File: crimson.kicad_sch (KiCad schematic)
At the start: 184 parts, among them J1 Conn_01x02_Socket, SW1 SW_Push_Shielded, SW10 SW_Push_Shielded, SW11 SW_Push_Shielded, SW12 SW_Push_Shielded, SW13 SW_Push_Shielded, SW14 SW_Push_Shielded, SW15 SW_Push_Shielded, SW16 SW_Push_Shielded, SW17 SW_Push_Shielded, SW18 SW_Push_Shielded, SW19 SW_Push_Shielded, SW2 SW_Push_Shielded, SW20 SW_Push_Shielded, SW21 SW_Push_Shielded, SW22 SW_Push_Shielded, SW23 SW_Push_Shielded, SW24 SW_Push_Shielded, SW25 SW_Push_Shielded, SW26 SW_Push_Shielded, SW27 SW_Push_Shielded, SW28 SW_Push_Shielded, SW29 SW_Push_Shielded, SW3 SW_Push_Shielded, SW30 SW_Push_Shielded, SW31 SW_Push_Shielded, SW32 SW_Push_Shielded, SW33 SW_Push_Shielded, SW34 SW_Push_Shielded, SW35 SW_Push_Shielded, SW36 SW_Push_Shielded, SW37 SW_Push_Shielded, SW38 SW_Push_Shielded, SW39 SW_Push_Shielded, SW4 SW_Push_Shielded, SW40 SW_Push_Shielded, SW41 SW_Push_Shielded, SW42 SW_Push_Shielded, SW43 SW_Push_Shielded, SW44 SW_Push_Shielded, SW45 SW_Push_Shielded, SW46 SW_Push_Shielded, SW47 SW_Push_Shielded, SW48 SW_Push_Shielded, SW49 SW_Push_Shielded, SW5 SW_Push_Shielded, SW50 SW_Push_Shielded, SW51 SW_Push_Shielded, SW52 SW_Push_Shielded, SW53 SW_Push_Shielded, SW54 SW_Push_Shielded, SW55 SW_Push_Shielded, SW56 SW_Push_Shielded, SW57 SW_Push_Shielded, SW58 SW_Push_Shielded, SW59 SW_Push_Shielded, SW6 SW_Push_Shielded, SW60 SW_Push_Shielded, SW61 SW_Push_Shielded, SW62 SW_Push_Shielded, SW63 SW_Push_Shielded, SW64 SW_Push_Shielded, SW65 SW_Push_Shielded, SW66 SW_Push_Shielded, SW67 SW_Push_Shielded, SW68 SW_Push_Shielded, SW69 SW_Push_Shielded, SW7 SW_Push_Shielded, SW70 SW_Push_Shielded, SW71 SW_Push_Shielded, SW72 SW_Push_Shielded, SW73 SW_Push_Shielded, SW74 SW_Push_Shielded, SW75 SW_Push_Shielded, SW76 SW_Push_Shielded, SW77 SW_Push_Shielded, SW78 SW_Push_Shielded, SW79 SW_Push_Shielded, SW8 SW_Push_Shielded, SW80 SW_Push_Shielded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

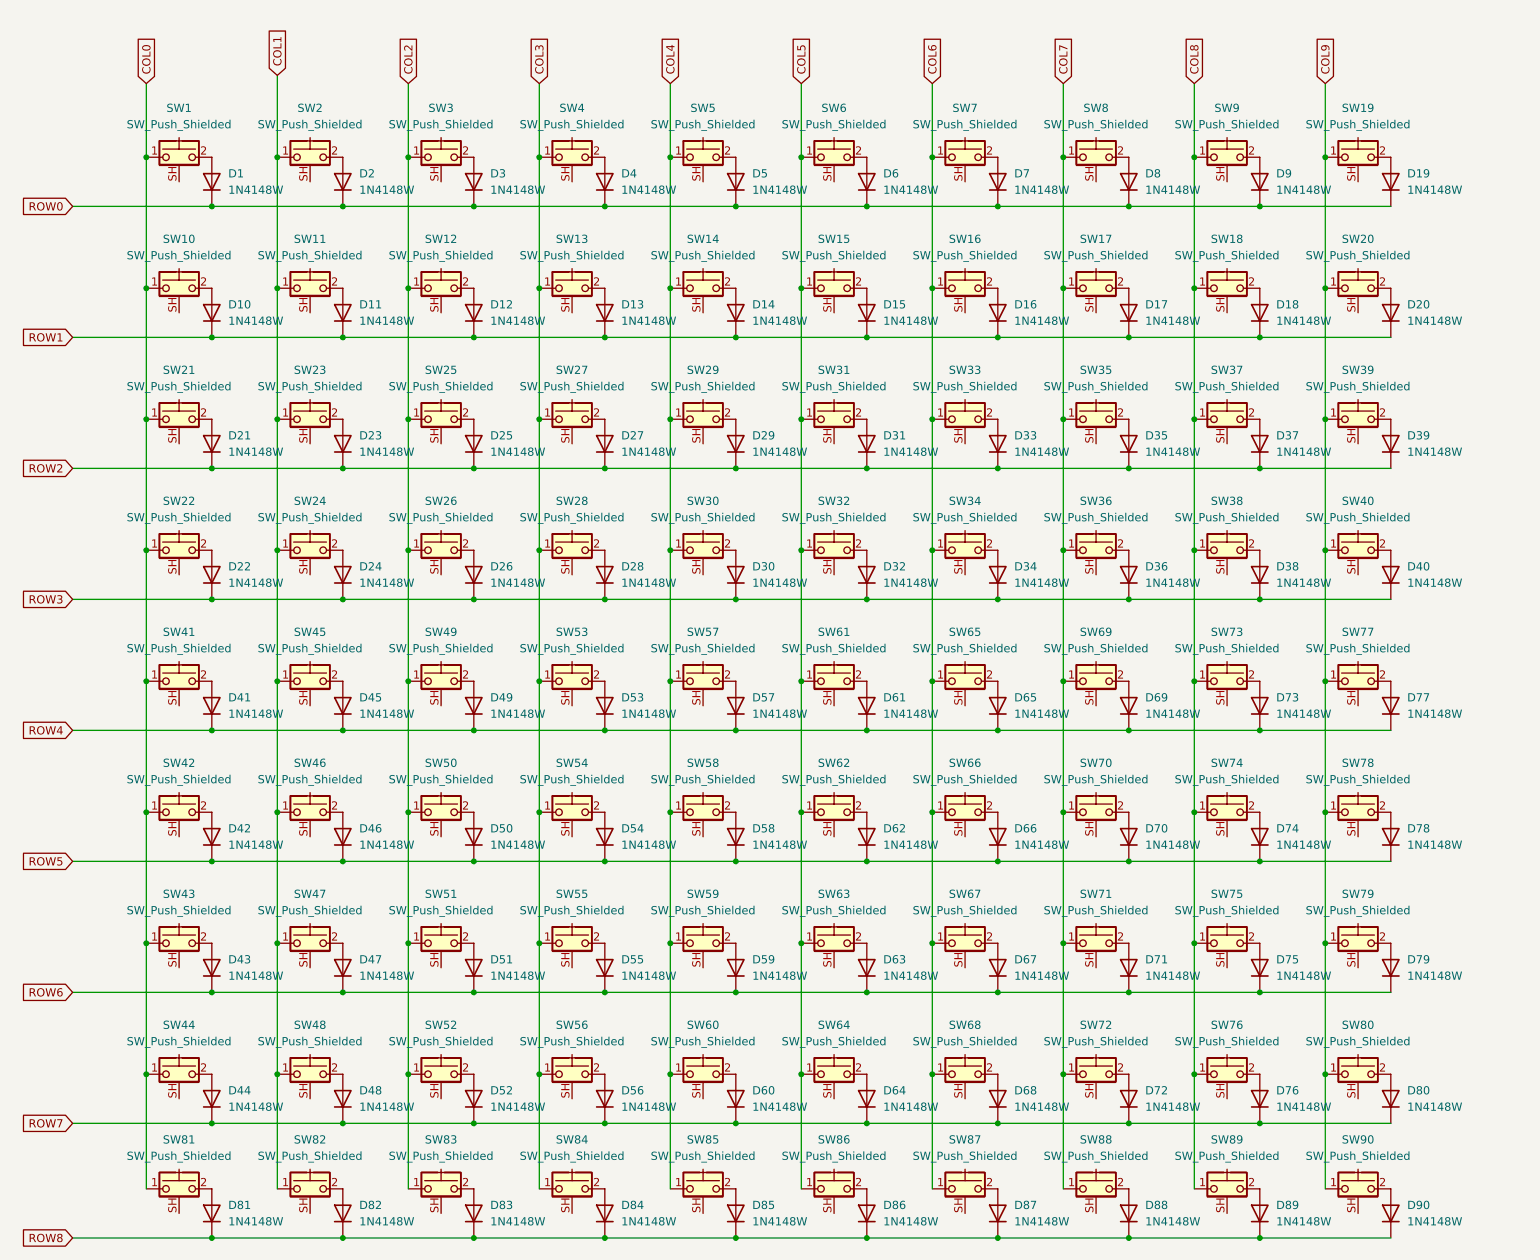
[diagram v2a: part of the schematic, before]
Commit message: [schematics] Add labels for default layout
Default layout will be ANSI QWERTY, so I labeled
the keys accordingly, just so I have a better overview
of things. Layout can be changed later on to stuff like
DVORAK or sth

Signed-off-by: Lucy Mielke <user@domain.tld>
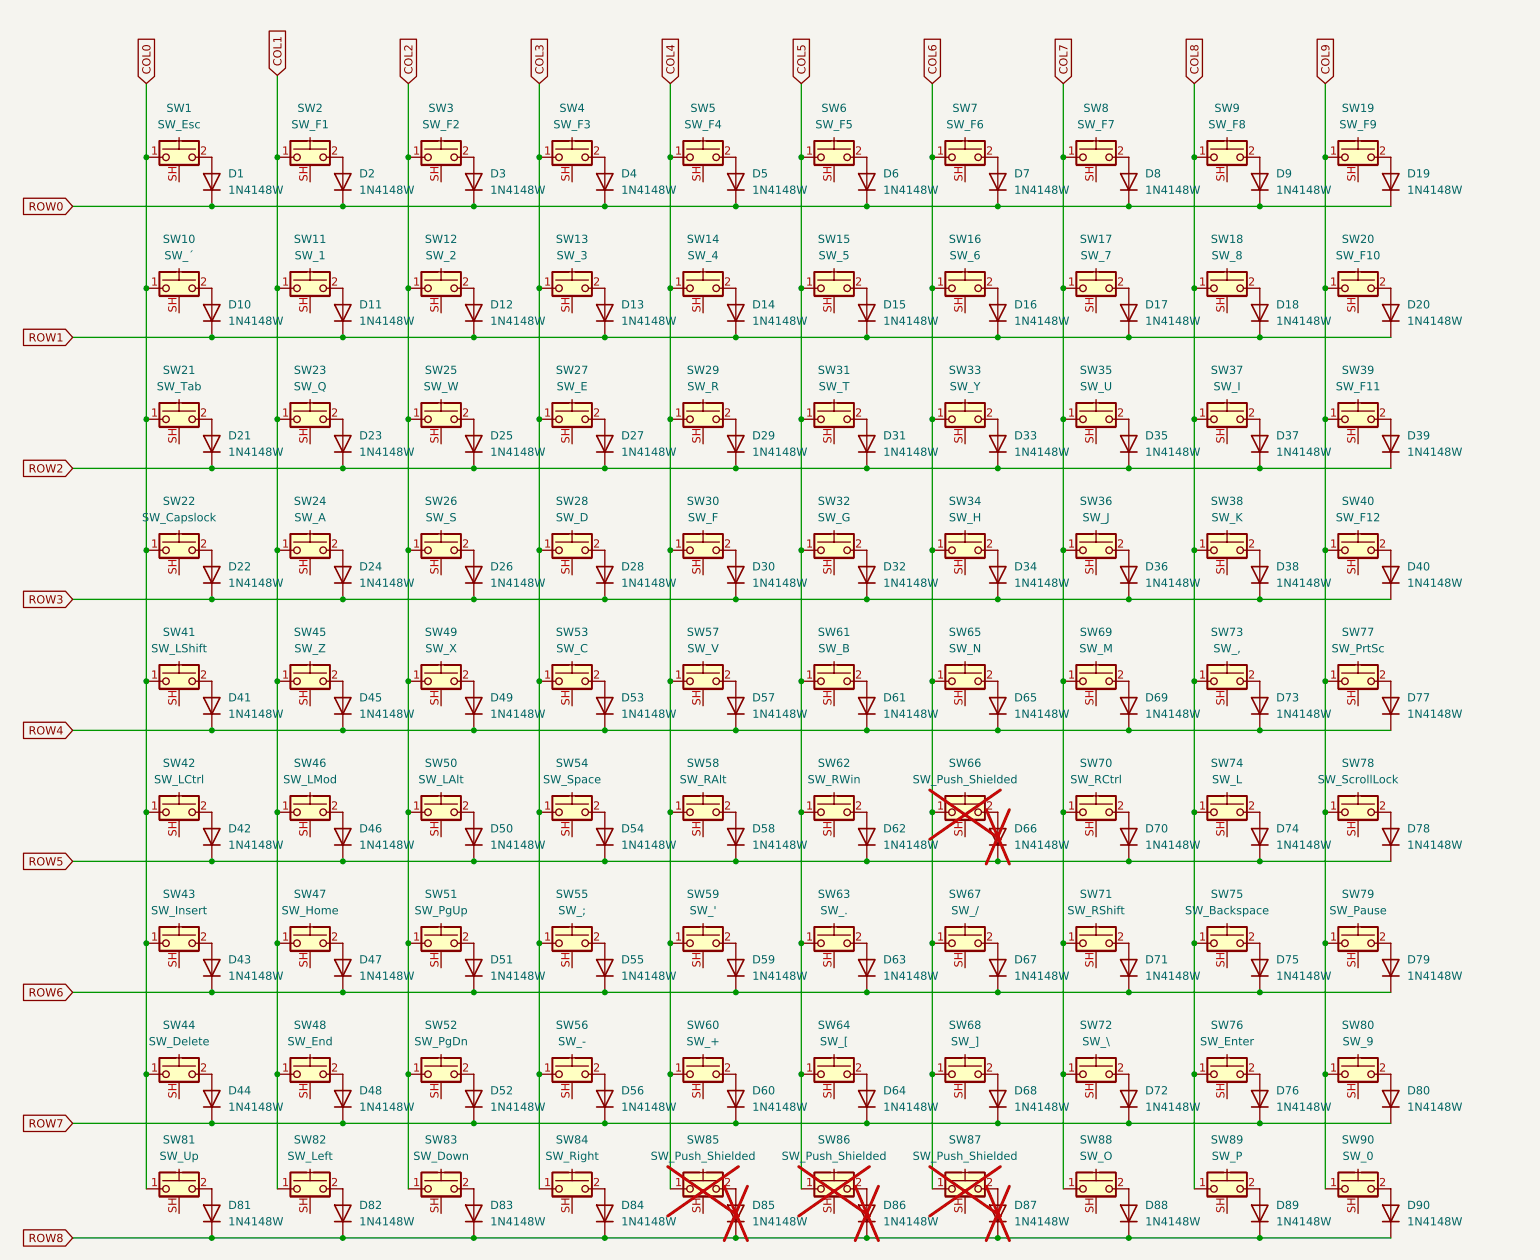
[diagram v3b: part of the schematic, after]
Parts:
- D66, D85, D86, D87, SW66, SW85, SW86, SW87: now not fitted
- SW1: value SW_Push_Shielded -> SW_Esc
- SW10: value SW_Push_Shielded -> SW_´
- SW11: value SW_Push_Shielded -> SW_1
- SW12: value SW_Push_Shielded -> SW_2
- SW13: value SW_Push_Shielded -> SW_3
- SW14: value SW_Push_Shielded -> SW_4
- SW15: value SW_Push_Shielded -> SW_5
- SW16: value SW_Push_Shielded -> SW_6
- SW17: value SW_Push_Shielded -> SW_7
- SW18: value SW_Push_Shielded -> SW_8
- SW19: value SW_Push_Shielded -> SW_F9
- SW2: value SW_Push_Shielded -> SW_F1
- SW20: value SW_Push_Shielded -> SW_F10
- SW21: value SW_Push_Shielded -> SW_Tab
- SW22: value SW_Push_Shielded -> SW_Capslock
- SW23: value SW_Push_Shielded -> SW_Q
- SW24: value SW_Push_Shielded -> SW_A
- SW25: value SW_Push_Shielded -> SW_W
- SW26: value SW_Push_Shielded -> SW_S
- SW27: value SW_Push_Shielded -> SW_E
- SW28: value SW_Push_Shielded -> SW_D
- SW29: value SW_Push_Shielded -> SW_R
- SW3: value SW_Push_Shielded -> SW_F2
- SW30: value SW_Push_Shielded -> SW_F
- SW31: value SW_Push_Shielded -> SW_T
- SW32: value SW_Push_Shielded -> SW_G
- SW33: value SW_Push_Shielded -> SW_Y
- SW34: value SW_Push_Shielded -> SW_H
- SW35: value SW_Push_Shielded -> SW_U
- SW36: value SW_Push_Shielded -> SW_J
- SW37: value SW_Push_Shielded -> SW_I
- SW38: value SW_Push_Shielded -> SW_K
- SW39: value SW_Push_Shielded -> SW_F11
- SW4: value SW_Push_Shielded -> SW_F3
- SW40: value SW_Push_Shielded -> SW_F12
- SW41: value SW_Push_Shielded -> SW_LShift
- SW42: value SW_Push_Shielded -> SW_LCtrl
- SW43: value SW_Push_Shielded -> SW_Insert
- SW44: value SW_Push_Shielded -> SW_Delete
- SW45: value SW_Push_Shielded -> SW_Z
- SW46: value SW_Push_Shielded -> SW_LMod
- SW47: value SW_Push_Shielded -> SW_Home
- SW48: value SW_Push_Shielded -> SW_End
- SW49: value SW_Push_Shielded -> SW_X
- SW5: value SW_Push_Shielded -> SW_F4
- SW50: value SW_Push_Shielded -> SW_LAlt
- SW51: value SW_Push_Shielded -> SW_PgUp
- SW52: value SW_Push_Shielded -> SW_PgDn
- SW53: value SW_Push_Shielded -> SW_C
- SW54: value SW_Push_Shielded -> SW_Space
- SW55: value SW_Push_Shielded -> SW_;
- SW56: value SW_Push_Shielded -> SW_-
- SW57: value SW_Push_Shielded -> SW_V
- SW58: value SW_Push_Shielded -> SW_RAlt
- SW59: value SW_Push_Shielded -> SW_'
- SW6: value SW_Push_Shielded -> SW_F5
- SW60: value SW_Push_Shielded -> SW_+
- SW61: value SW_Push_Shielded -> SW_B
- SW62: value SW_Push_Shielded -> SW_RWin
- SW63: value SW_Push_Shielded -> SW_.
- SW64: value SW_Push_Shielded -> SW_[
- SW65: value SW_Push_Shielded -> SW_N
- SW67: value SW_Push_Shielded -> SW_/
- SW68: value SW_Push_Shielded -> SW_]
- SW69: value SW_Push_Shielded -> SW_M
- SW7: value SW_Push_Shielded -> SW_F6
- SW70: value SW_Push_Shielded -> SW_RCtrl
- SW71: value SW_Push_Shielded -> SW_RShift
- SW72: value SW_Push_Shielded -> SW_\
- SW73: value SW_Push_Shielded -> SW_,
- SW74: value SW_Push_Shielded -> SW_L
- SW75: value SW_Push_Shielded -> SW_Backspace
- SW76: value SW_Push_Shielded -> SW_Enter
- SW77: value SW_Push_Shielded -> SW_PrtSc
- SW78: value SW_Push_Shielded -> SW_ScrollLock
- SW79: value SW_Push_Shielded -> SW_Pause
- SW8: value SW_Push_Shielded -> SW_F7
- SW80: value SW_Push_Shielded -> SW_9
- SW81: value SW_Push_Shielded -> SW_Up
- SW82: value SW_Push_Shielded -> SW_Left
- SW83: value SW_Push_Shielded -> SW_Down
- SW84: value SW_Push_Shielded -> SW_Right
- SW88: value SW_Push_Shielded -> SW_O
- SW89: value SW_Push_Shielded -> SW_P
- SW9: value SW_Push_Shielded -> SW_F8
- SW90: value SW_Push_Shielded -> SW_0

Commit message: [pcb] first attempt regarding switch placement
Everything except the diodes have been arranged for the first time.

Signed-off-by: Lucy Mielke <user@domain.tld>
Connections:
- net GND: now also SW1.SH (B), SW10.SH (B), SW11.SH (B), SW12.SH (B), SW13.SH (B), SW14.SH (B), SW15.SH (B), SW16.SH (B), SW17.SH (B), SW18.SH (B), SW19.SH (B), SW2.SH (B), SW20.SH (B), SW21.SH (B), SW22.SH (B), SW23.SH (B), SW24.SH (B), SW25.SH (B), SW26.SH (B), SW27.SH (B), SW28.SH (B), SW29.SH (B), SW3.SH (B), SW30.SH (B), SW31.SH (B), SW32.SH (B), SW33.SH (B), SW34.SH (B), SW35.SH (B), SW36.SH (B), SW37.SH (B), SW38.SH (B), SW39.SH (B), SW4.SH (B), SW40.SH (B), SW41.SH (B), SW42.SH (B), SW43.SH (B), SW44.SH (B), SW45.SH (B), SW46.SH (B), SW47.SH (B), SW48.SH (B), SW49.SH (B), SW5.SH (B), SW50.SH (B), SW51.SH (B), SW52.SH (B), SW53.SH (B), SW54.SH (B), SW55.SH (B), SW56.SH (B), SW57.SH (B), SW58.SH (B), SW59.SH (B), SW6.SH (B), SW60.SH (B), SW61.SH (B), SW62.SH (B), SW63.SH (B), SW64.SH (B), SW65.SH (B), SW66.SH (B), SW67.SH (B), SW68.SH (B), SW69.SH (B), SW7.SH (B), SW70.SH (B), SW71.SH (B), SW72.SH (B), SW73.SH (B), SW74.SH (B), SW75.SH (B), SW76.SH (B), SW77.SH (B), SW78.SH (B), SW79.SH (B), SW8.SH (B), SW80.SH (B), SW81.SH (B), SW82.SH (B), SW83.SH (B), SW84.SH (B), SW85.SH (B), SW86.SH (B), SW87.SH (B), SW88.SH (B), SW89.SH (B), SW9.SH (B), SW90.SH (B)

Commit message: [misc] add graphics and instructions for future non-exhausted me
I am tired, have a headache, and can't think straight. This is left for
future me to take care of

REMINDER: U still need mounting holes bruh

Signed-off-by: Lucy Mielke <user@domain.tld>
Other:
- note added: "Left half: COL0-COL3 + COL5, ROW0-ROW5, ROW8"

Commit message: [schematic] seperate left third and mid third, connect them with pogo pins
The left and middle thirds are now electrically disconnected with each
other for foldability.

The two thirds are going to be electrically connected via pogo pins
instead, allowing for easily making and breaking the electric
connections.

The right third still needs to be done. Only after that has been done,
the final layout can be made, including adding mounting holes and such.

Signed-off-by: Lucy Mielke <user@domain.tld>
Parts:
- added J2, J3, J4, J5: Conn_01x04_Pin, symbol Connector:Conn_01x04_Pin
- added J6, J7, J8, J9: Conn_01x04_Socket, symbol Connector:Conn_01x04_Socket
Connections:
- net COL0: now also J4.4 (Pin_4); no longer SW43.1, SW44.1, SW81.1
- net COL1: now also J4.3 (Pin_3); no longer SW47.1, SW48.1, SW82.1
- net COL2: now also J4.2 (Pin_2); no longer SW51.1, SW52.1, SW83.1
- net COL3: now also J8.1 (Pin_1); no longer SW13.1, SW27.1, SW28.1, SW53.1, SW54.1, SW55.1, SW56.1, SW84.1
- net COL5: now also J9.3 (Pin_3); no longer SW86.1
- net GND: now also J3.1 (Pin_1), J5.1 (Pin_1), J7.1 (Pin_1), J9.1 (Pin_1)
- net ROW0: now also J2.4 (Pin_4); no longer D19.1 (K), D4.1 (K), D5.1 (K), D6.1 (K), D7.1 (K), D8.1 (K), D9.1 (K)
- net ROW1: now also J2.3 (Pin_3); no longer D14.1 (K), D15.1 (K), D16.1 (K), D17.1 (K), D18.1 (K), D20.1 (K)
- net ROW2: now also J2.2 (Pin_2); no longer D29.1 (K), D31.1 (K), D33.1 (K), D35.1 (K), D37.1 (K), D39.1 (K)
- net ROW3: now also J2.1 (Pin_1); no longer D30.1 (K), D32.1 (K), D34.1 (K), D36.1 (K), D38.1 (K), D40.1 (K)
- net ROW4: now also J3.4 (Pin_4); no longer D57.1 (K), D61.1 (K), D65.1 (K), D69.1 (K), D73.1 (K), D77.1 (K)
- net ROW5: now also J3.3 (Pin_3); no longer D54.1 (K), D58.1 (K), D62.1 (K), D66.1 (K), D70.1 (K), D74.1 (K), D78.1 (K)
- net ROW8: now also J7.2 (Pin_2); no longer D86.1 (K), D87.1 (K), D88.1 (K), D89.1 (K), D90.1 (K)
- new net col0_mid: J8.4 (Pin_4), SW43.1, SW44.1, SW81.1
- new net col1_mid: J8.3 (Pin_3), SW47.1, SW48.1, SW82.1
- new net col2_mid: J8.2 (Pin_2), SW51.1, SW52.1, SW83.1
- new net col3_left_in: J4.1 (Pin_1), J5.4 (Pin_4), SW13.1, SW27.1, SW28.1, SW53.1
- new net col3_mid_out: J9.4 (Pin_4), SW54.1, SW55.1, SW56.1, SW84.1
- new net col5_left: J5.3 (Pin_3), SW86.1
- new net row0_mid: D19.1 (K), D4.1 (K), D5.1 (K), D6.1 (K), D7.1 (K), D8.1 (K), D9.1 (K), J6.4 (Pin_4)
- new net row1_mid: D14.1 (K), D15.1 (K), D16.1 (K), D17.1 (K), D18.1 (K), D20.1 (K), J6.3 (Pin_3)
- new net row2_mid: D29.1 (K), D31.1 (K), D33.1 (K), D35.1 (K), D37.1 (K), D39.1 (K), J6.2 (Pin_2)
- new net row3_mid: D30.1 (K), D32.1 (K), D34.1 (K), D36.1 (K), D38.1 (K), D40.1 (K), J6.1 (Pin_1)
- new net row4_mid: D57.1 (K), D61.1 (K), D65.1 (K), D69.1 (K), D73.1 (K), D77.1 (K), J7.4 (Pin_4)
- new net row5_mid: D54.1 (K), D58.1 (K), D62.1 (K), D66.1 (K), D70.1 (K), D74.1 (K), D78.1 (K), J7.3 (Pin_3)
- new net row8_left_in: D86.1 (K), J3.2 (Pin_2), J5.2 (Pin_2)
- new net row8_mid_out: D87.1 (K), D88.1 (K), D89.1 (K), D90.1 (K), J9.2 (Pin_2)
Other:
- note added: "COL5"
- note added: "Left half: COL0-COL3 + COL5, ROW0-ROW5 + ROW8"
- note added: "ROW8"
- note removed: "Left half: COL0-COL3 + COL5, ROW0-ROW5, ROW8"
- moved on the sheet: D1, D10, D11, D12, D13, D14, D15, D16, D17, D18, D19, D2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
